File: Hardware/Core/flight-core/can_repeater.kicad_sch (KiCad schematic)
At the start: 9 parts, among them U5 TCAN1042HGVDRQ1

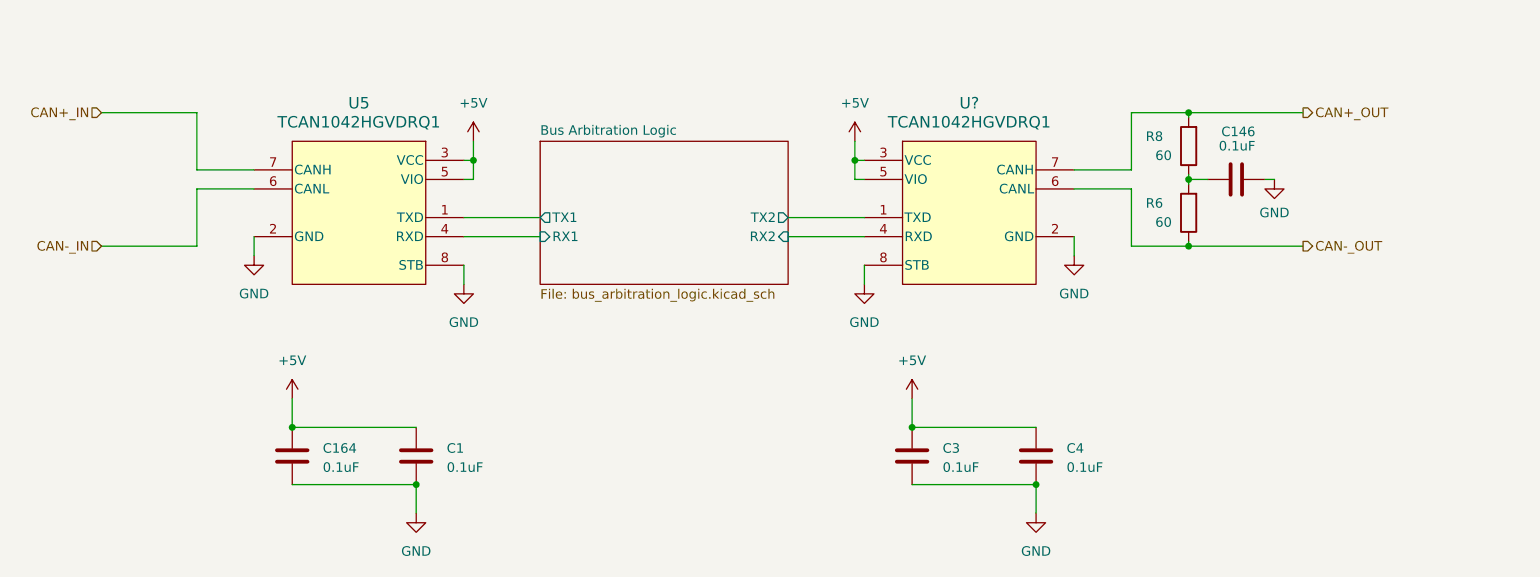
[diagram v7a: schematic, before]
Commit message: minor erc fixes (grid, reannotation, updated footprint associations)
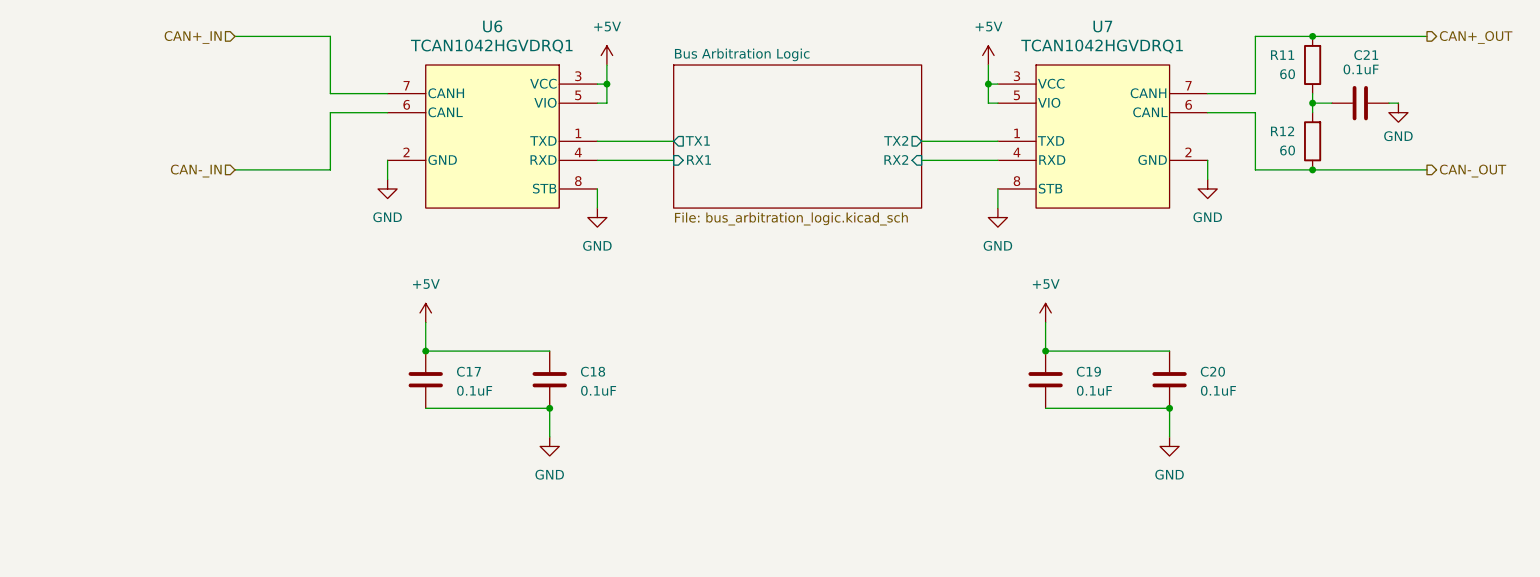
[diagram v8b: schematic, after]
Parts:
- gave numbers to parts that had none: 1
- renumbered C164 to C17, C1 to C18, C3 to C19, C4 to C20, C146 to C21, R8 to R11, R6 to R12, U5 to U6
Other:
- moved on the sheet: C17, C18, C19, C20, C21, R11, R12, U6, U7
